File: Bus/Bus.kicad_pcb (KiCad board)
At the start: 2 copper layers, 89.9 x 120.4 mm, 31 parts, among them J1 Conn_01x22, J2 Conn_01x22, J3 Conn_01x22, J4 Conn_01x22, J5 Conn_01x16, J6 Conn_01x16, J7 Conn_01x16, J8 Conn_01x16, U1 74LS139, U2 SN74LS04N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

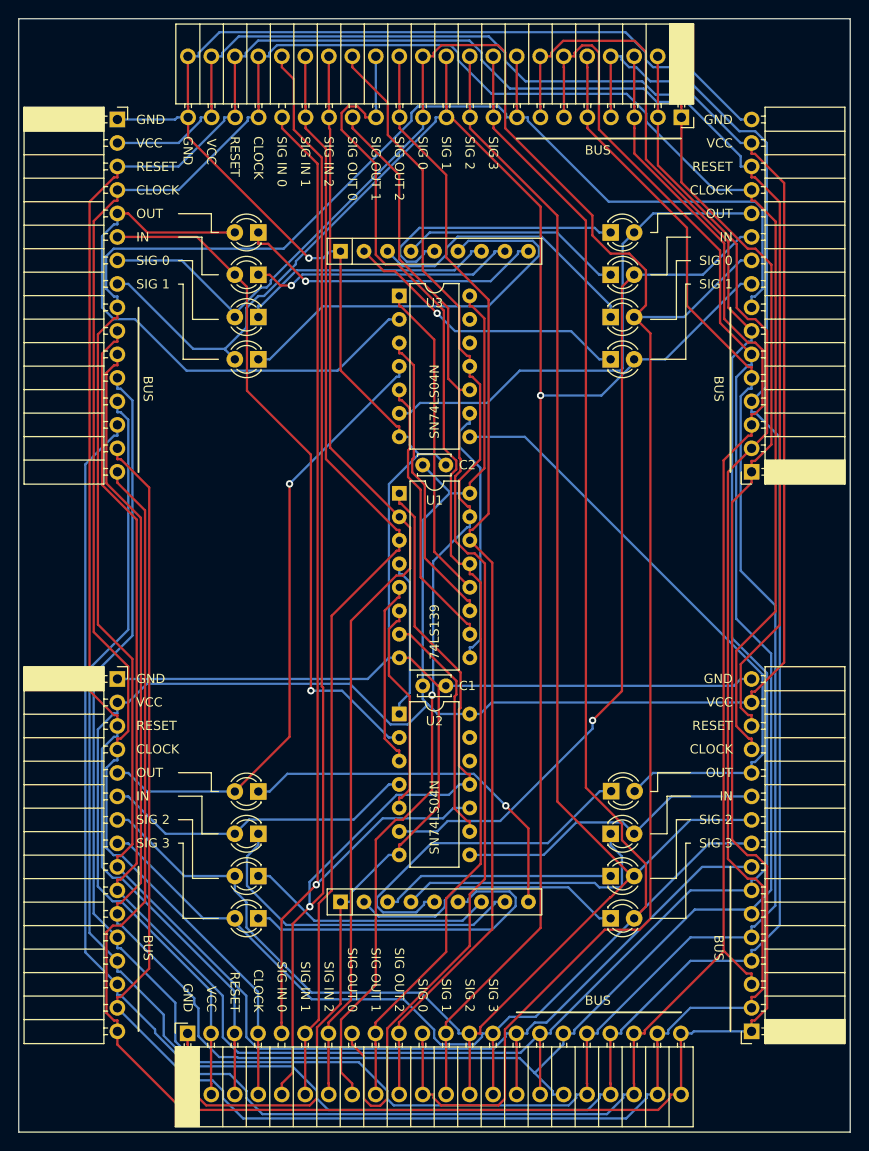
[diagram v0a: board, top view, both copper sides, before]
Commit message: Fixed floating inputs; improved power; added parts list; replaced JK latches
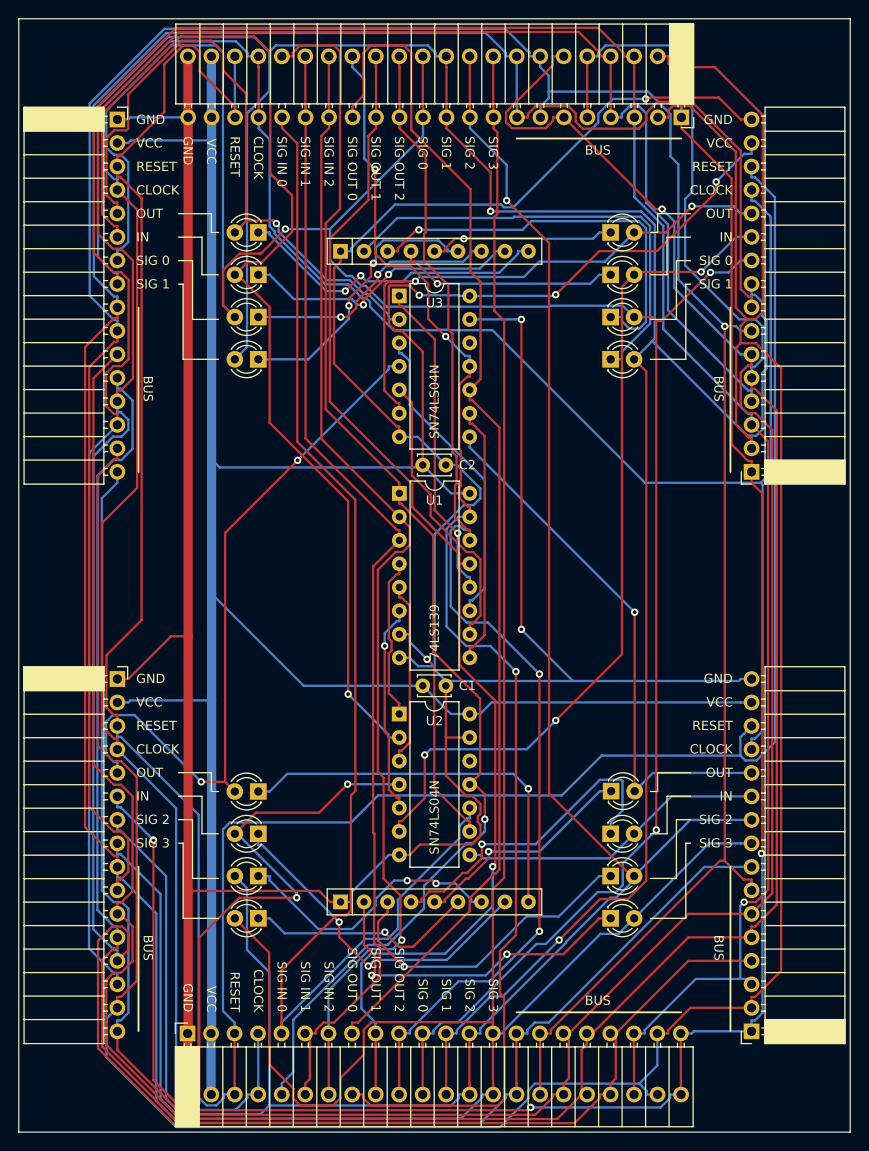
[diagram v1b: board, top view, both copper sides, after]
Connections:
- U2 pad 13: Net-(U2-Pad13) -> GND
- U3 pad 13: Net-(U3-Pad13) -> GND
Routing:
- net GND: track 302.5 -> 382.9 mm, vias 1 -> 3
- net SIG1: track 201.4 -> 275.5 mm, vias 1 -> 2
- net SIG3: track 194.8 -> 268.7 mm
- net MODULE_IN_1: track 34.4 -> 98.8 mm, vias 0 -> 3
- net BUS6: track 259.8 -> 313.8 mm
- net MODULE_IN_0: track 74.4 -> 123.2 mm
- net RESET: track 260.4 -> 307.1 mm
- net SIG2: track 193.4 -> 237.0 mm, vias 0 -> 1
- net BUS4: track 272.7 -> 311.7 mm
- net CLOCK: track 260.6 -> 298.7 mm
- net BUS5: track 258.3 -> 295.8 mm, vias 0 -> 1
- net SIG_IN_0: track 175.4 -> 140.8 mm
- net BUS0: track 266.0 -> 300.2 mm
- net SIG0: track 224.4 -> 257.3 mm, vias 0 -> 3
- net VCC: track 322.6 -> 296.0 mm, vias 0 -> 3
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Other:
- rule pad_to_mask_clearance: 0.051 -> 0

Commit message: Update all boards to r3, and update revision log and gitignore
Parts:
- added HOLE1: MountingHole_2.2mm_M2_DIN965_Pad, MountingHole:MountingHole_2.2mm_M2_DIN965_Pad, F.Cu at (54.9, 54.9)
- added HOLE2: MountingHole_2.2mm_M2_DIN965_Pad, MountingHole:MountingHole_2.2mm_M2_DIN965_Pad, F.Cu at (136.7, 55.1)
- added HOLE3: MountingHole_2.2mm_M2_DIN965_Pad, MountingHole:MountingHole_2.2mm_M2_DIN965_Pad, F.Cu at (54.9, 167.1)
- added HOLE4: MountingHole_2.2mm_M2_DIN965_Pad, MountingHole:MountingHole_2.2mm_M2_DIN965_Pad, F.Cu at (136.7, 167.1)
- U1: value 74LS139 -> 74HC139
- U2, U3: value SN74LS04N -> SN74HC04N
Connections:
- net ~SIG_IN_0 renamed ~{SIG_IN_0}
- net ~SIG_OUT_0 renamed ~{SIG_OUT_0}
- U2 pad 12: Net-(U2-Pad12) -> unconnected-(U2-6Y-Pad12)
- U3 pad 12: Net-(U3-Pad12) -> unconnected-(U3-6Y-Pad12)
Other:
- net class Default removed

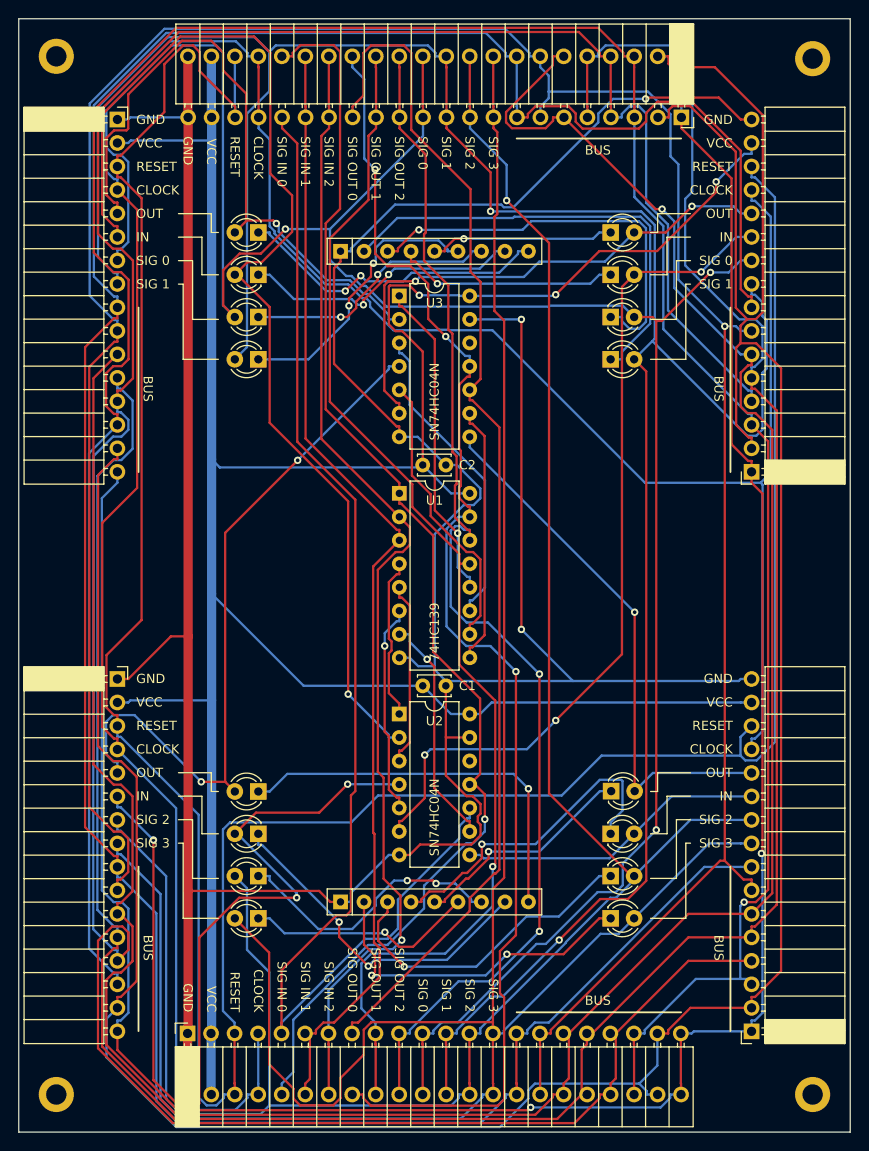
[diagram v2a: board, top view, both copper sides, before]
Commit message: Make bus board 4L with ground planes and extra GND connectors
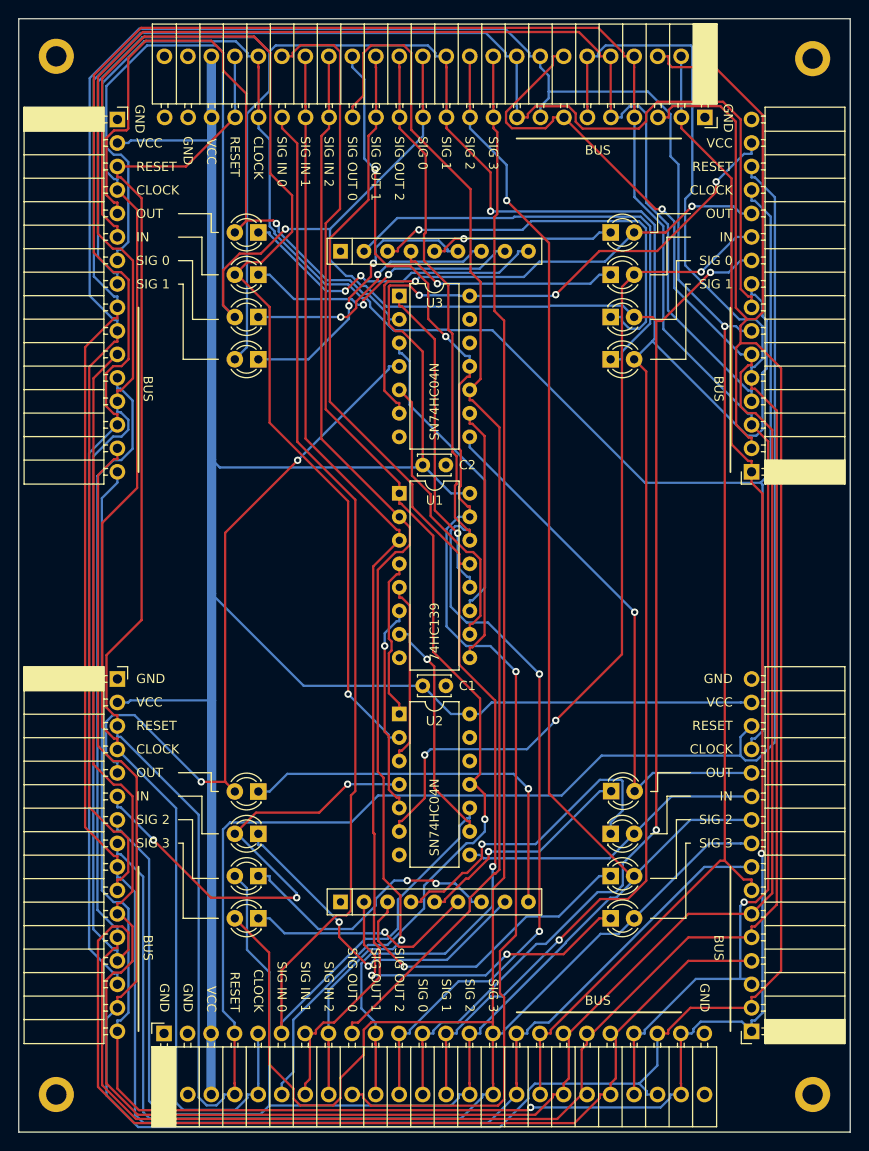
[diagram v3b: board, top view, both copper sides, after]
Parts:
- J1, J3: value Conn_01x22 -> Conn_01x24; footprint Connector_PinHeader_2.54mm:PinHeader_1x22_P2.54mm_Horizontal -> Connector_PinHeader_2.54mm:PinHeader_1x24_P2.54mm_Horizontal
- J2, J4: value Conn_01x22 -> Conn_01x24; footprint Connector_PinSocket_2.54mm:PinSocket_1x22_P2.54mm_Horizontal -> Connector_PinSocket_2.54mm:PinSocket_1x24_P2.54mm_Horizontal
- moved J2 2.54 mm to (125.0, 61.5)
- moved J4 2.54 mm to (66.5, 160.5)
- moved J1 2.54 mm to (125.0, 54.9)
- moved J3 2.54 mm to (66.5, 167.1)
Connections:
- J1 pad 1: BUS7 -> GND
- J1 pad 10: SIG2 -> SIG3
- J1 pad 11: SIG1 -> SIG2
- J1 pad 12: SIG0 -> SIG1
- J1 pad 13: SIG_OUT_2 -> SIG0
- J1 pad 14: SIG_OUT_1 -> SIG_OUT_2
- J1 pad 15: SIG_OUT_0 -> SIG_OUT_1
- J1 pad 16: SIG_IN_2 -> SIG_OUT_0
- J1 pad 17: SIG_IN_1 -> SIG_IN_2
- J1 pad 18: SIG_IN_0 -> SIG_IN_1
- J1 pad 19: CLOCK -> SIG_IN_0
- J1 pad 2: BUS6 -> BUS7
- J1 pad 20: RESET -> CLOCK
- J1 pad 21: VCC -> RESET
- J1 pad 22: GND -> VCC
- J1 pad 3: BUS5 -> BUS6
- J1 pad 4: BUS4 -> BUS5
- J1 pad 5: BUS3 -> BUS4
- J1 pad 6: BUS2 -> BUS3
- J1 pad 7: BUS1 -> BUS2
- J1 pad 8: BUS0 -> BUS1
- J1 pad 9: SIG3 -> BUS0
- J2 pad 1: BUS7 -> GND
- J2 pad 10: SIG2 -> SIG3
- J2 pad 11: SIG1 -> SIG2
- J2 pad 12: SIG0 -> SIG1
- J2 pad 13: SIG_OUT_2 -> SIG0
- J2 pad 14: SIG_OUT_1 -> SIG_OUT_2
- J2 pad 15: ~{SIG_OUT_0} -> SIG_OUT_1
- J2 pad 16: SIG_IN_2 -> ~{SIG_OUT_0}
- J2 pad 17: SIG_IN_1 -> SIG_IN_2
- J2 pad 18: ~{SIG_IN_0} -> SIG_IN_1
- J2 pad 19: CLOCK -> ~{SIG_IN_0}
- J2 pad 2: BUS6 -> BUS7
- J2 pad 20: RESET -> CLOCK
- J2 pad 21: VCC -> RESET
- J2 pad 22: GND -> VCC
- J2 pad 3: BUS5 -> BUS6
- J2 pad 4: BUS4 -> BUS5
- J2 pad 5: BUS3 -> BUS4
- J2 pad 6: BUS2 -> BUS3
- J2 pad 7: BUS1 -> BUS2
- J2 pad 8: BUS0 -> BUS1
- J2 pad 9: SIG3 -> BUS0
- J3 pad 10: SIG_OUT_2 -> SIG_OUT_1
- J3 pad 11: SIG0 -> SIG_OUT_2
- J3 pad 12: SIG1 -> SIG0
- J3 pad 13: SIG2 -> SIG1
- J3 pad 14: SIG3 -> SIG2
- J3 pad 15: BUS0 -> SIG3
- J3 pad 16: BUS1 -> BUS0
- J3 pad 17: BUS2 -> BUS1
- J3 pad 18: BUS3 -> BUS2
- J3 pad 19: BUS4 -> BUS3
- J3 pad 2: VCC -> GND
- J3 pad 20: BUS5 -> BUS4
- J3 pad 21: BUS6 -> BUS5
- J3 pad 22: BUS7 -> BUS6
- J3 pad 3: RESET -> VCC
- J3 pad 4: CLOCK -> RESET
- J3 pad 5: SIG_IN_0 -> CLOCK
- J3 pad 6: SIG_IN_1 -> SIG_IN_0
- J3 pad 7: SIG_IN_2 -> SIG_IN_1
- J3 pad 8: SIG_OUT_0 -> SIG_IN_2
- J3 pad 9: SIG_OUT_1 -> SIG_OUT_0
- J4 pad 10: SIG_OUT_2 -> SIG_OUT_1
- J4 pad 11: SIG0 -> SIG_OUT_2
- J4 pad 12: SIG1 -> SIG0
- J4 pad 13: SIG2 -> SIG1
- J4 pad 14: SIG3 -> SIG2
- J4 pad 15: BUS0 -> SIG3
- J4 pad 16: BUS1 -> BUS0
- J4 pad 17: BUS2 -> BUS1
- J4 pad 18: BUS3 -> BUS2
- J4 pad 19: BUS4 -> BUS3
- J4 pad 2: VCC -> GND
- J4 pad 20: BUS5 -> BUS4
- J4 pad 21: BUS6 -> BUS5
- J4 pad 22: BUS7 -> BUS6
- J4 pad 3: RESET -> VCC
- J4 pad 4: CLOCK -> RESET
- J4 pad 5: ~{SIG_IN_0} -> CLOCK
- J4 pad 6: SIG_IN_1 -> ~{SIG_IN_0}
- J4 pad 7: SIG_IN_2 -> SIG_IN_1
- J4 pad 8: ~{SIG_OUT_0} -> SIG_IN_2
- J4 pad 9: SIG_OUT_1 -> ~{SIG_OUT_0}
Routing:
- net GND: track 382.9 -> 0.00 mm, vias 3 -> 0
- net MODULE_IN_1: track 98.8 -> 54.5 mm
- net RESET: track 307.1 -> 295.0 mm
- net BUS0: track 300.2 -> 305.8 mm
- net BUS4: track 311.7 -> 316.4 mm
- net BUS6: track 313.8 -> 318.1 mm
- net BUS7: track 254.6 -> 258.1 mm
- net BUS2: track 284.5 -> 287.0 mm
- net BUS3: track 286.5 -> 288.9 mm
- net MODULE_OUT_0: track 71.2 -> 73.5 mm
- net MODULE_IN_0: track 123.2 -> 125.5 mm
- net BUS5: track 295.8 -> 298.0 mm
- net SIG3: track 268.7 -> 270.6 mm
- net CLOCK: track 298.7 -> 300.3 mm
- net SIG1: track 275.5 -> 277.1 mm
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- added copper zone on In1.Cu, net GND
- added copper zone on In2.Cu, net GND
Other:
- copper layers 2 -> 4
